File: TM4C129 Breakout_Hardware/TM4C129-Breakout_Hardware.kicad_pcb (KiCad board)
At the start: 2 copper layers, 63.5 x 47 mm, 51 parts, among them J1 RJ45, J2 Conn_02x08, J3 Conn_02x08, J4 Conn_02x08, J5 Conn_02x02, J6 Conn_02x02, SW1 Reset, U1 HX1198FNL, U2 TM4C129ENCPDT, Y1 NX3225GA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

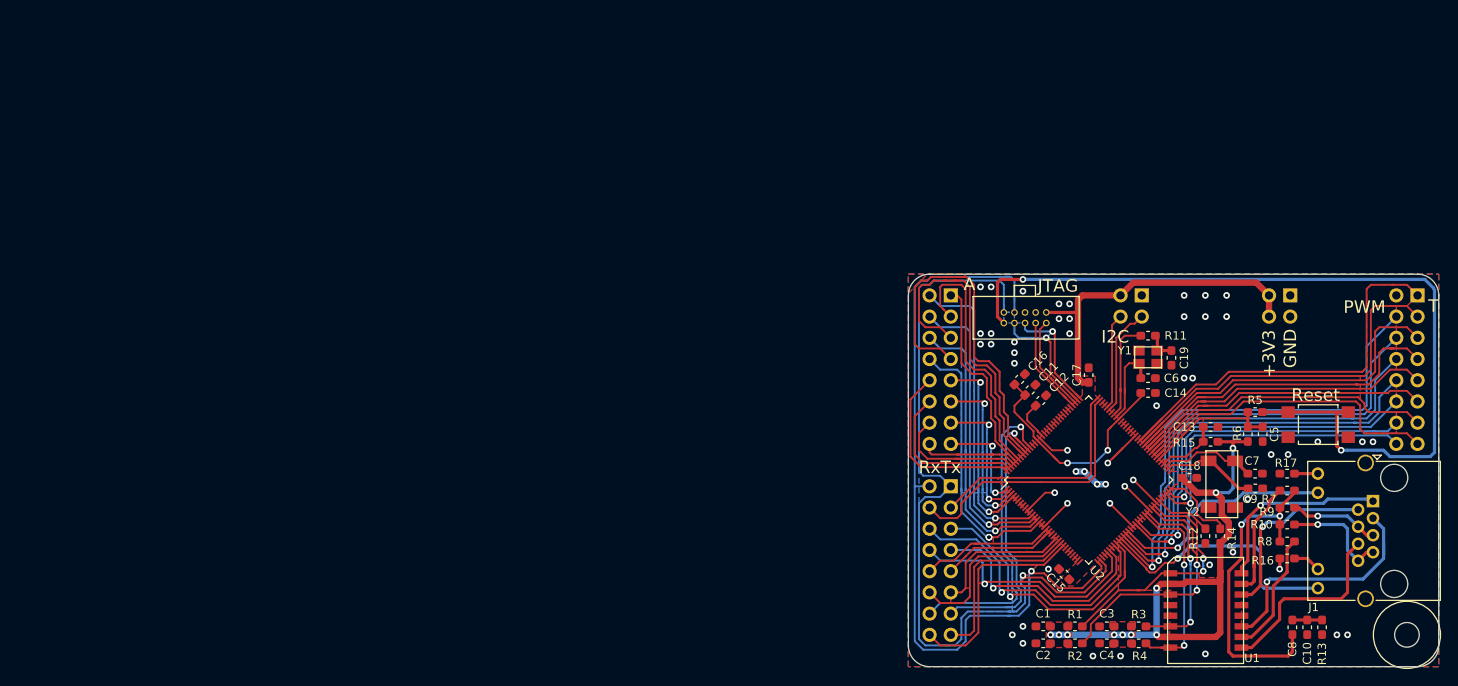
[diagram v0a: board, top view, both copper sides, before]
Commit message: updated TM4c layout
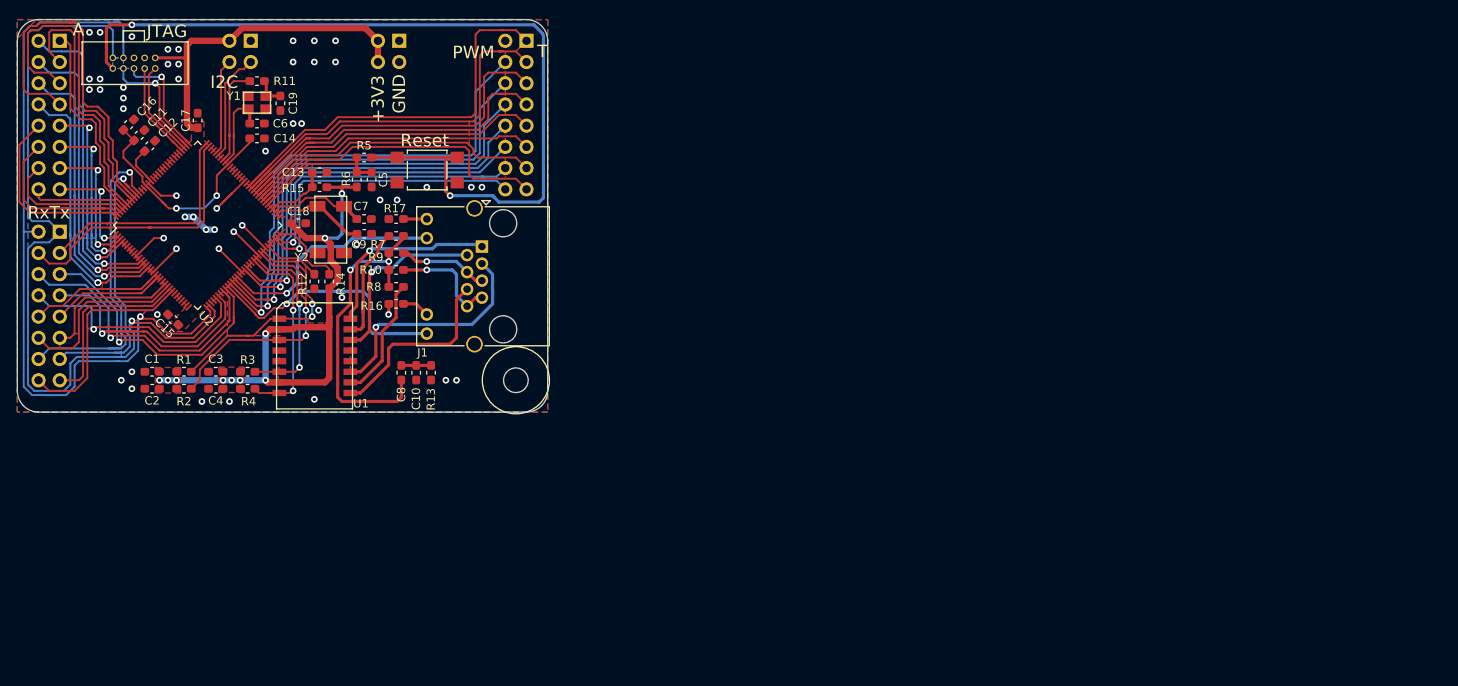
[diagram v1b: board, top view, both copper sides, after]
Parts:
- moved C1 110.9 mm to (13.6, 39.6)
- moved C11 110.9 mm to (12.0, 11.3)
- moved C13 110.9 mm to (33.6, 15.7)
- moved C14 110.9 mm to (26.2, 11.7)
- moved C16 110.9 mm to (10.8, 10.0)
- moved C17 110.9 mm to (19.1, 9.54)
- moved C18 110.9 mm to (31.1, 21.8)
- moved C2 110.9 mm to (13.6, 41.7)
- moved C3 110.9 mm to (21.2, 39.6)
- moved C4 110.9 mm to (21.2, 41.7)
- moved C6 110.9 mm to (26.2, 9.91)
- moved C7 110.9 mm to (39.0, 21.3)
- moved C8 110.9 mm to (43.4, 39.7)
- moved Conn1 110.9 mm to (14.0, 2.03)
- moved G*** 110.9 mm to (19.8, 19.7)
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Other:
- outline, holes or cut-outs redrawn
